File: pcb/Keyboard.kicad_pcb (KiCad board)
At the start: 2 copper layers, 166.7 x 94.8 mm, 63 parts

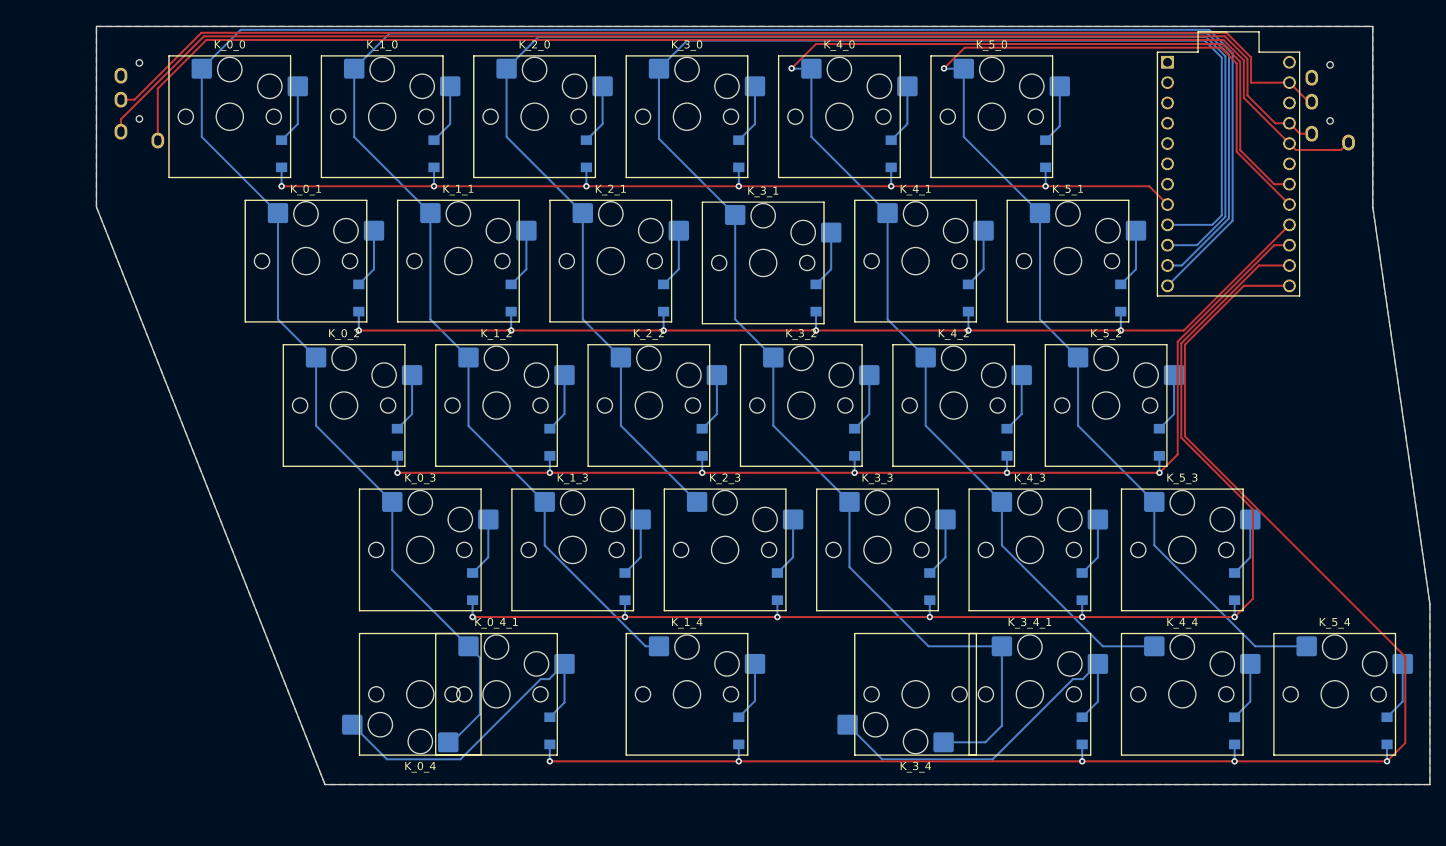
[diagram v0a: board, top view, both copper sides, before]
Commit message: Fix TRRS jack wiring.
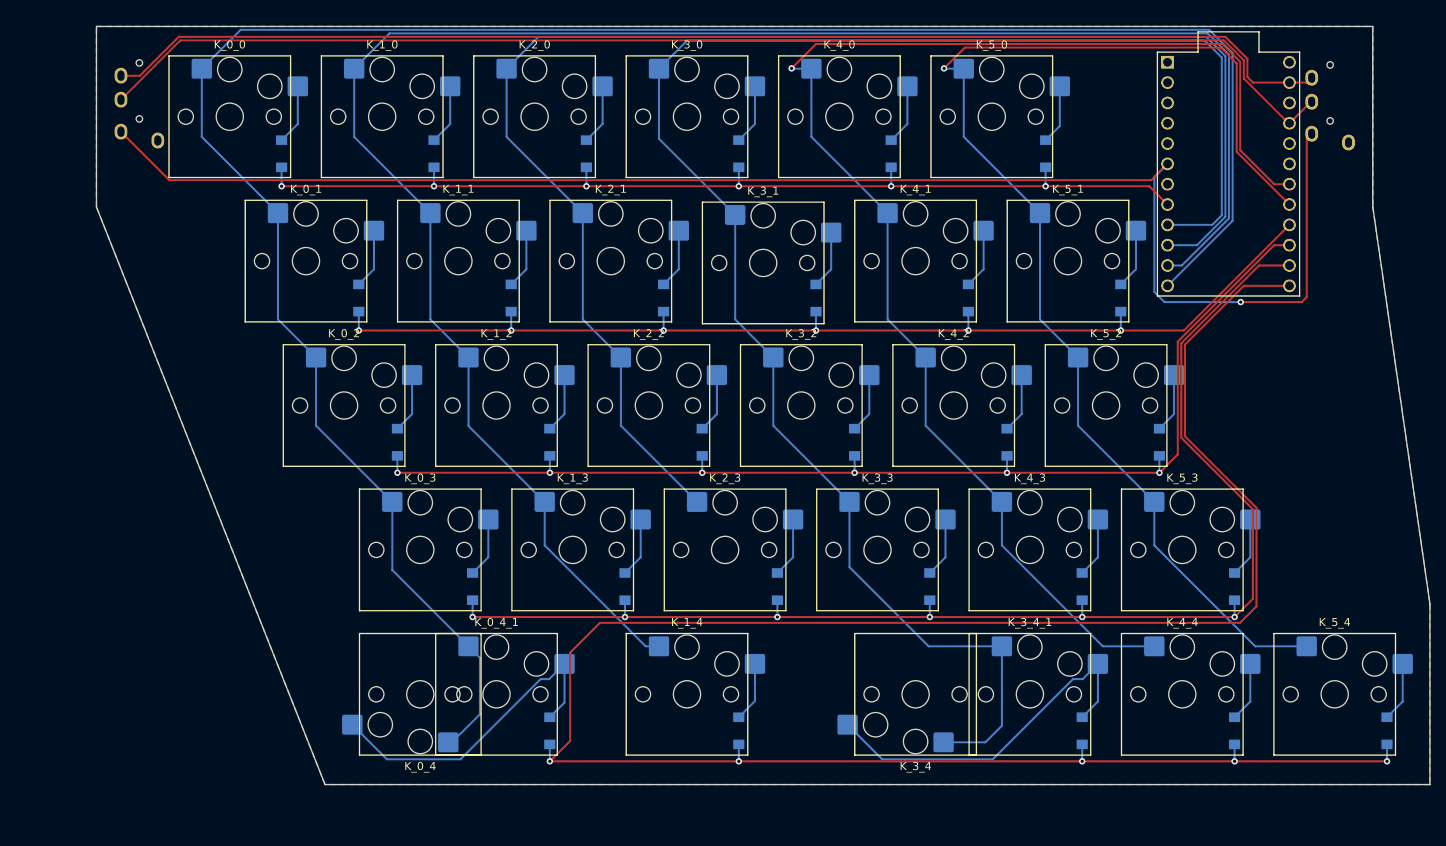
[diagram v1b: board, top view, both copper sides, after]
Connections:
- U_PROMICRO1 pad 20: Net-(U_PROMICRO1-Pad20) -> unconnected-(U_PROMICRO1-Pad20)
- U_PROMICRO1 pad 21: Net-(U_PROMICRO1-Pad21) -> trrs1
- U_PROMICRO1 pad 23: Net-(U_PROMICRO1-Pad23) -> trrs2
- U_PROMICRO1 pad 6: unconnected-(U_PROMICRO1-Pad6) -> trrs0
- U_TRRS1 pad 1: Net-(U_PROMICRO1-Pad20) -> unconnected-(U_TRRS1-Pad1)
- U_TRRS1 pad 2: Net-(U_PROMICRO1-Pad21) -> trrs0
- U_TRRS1 pad 3: Net-(U_PROMICRO1-Pad23) -> trrs1
- U_TRRS1 pad 4: unconnected-(U_TRRS1-Pad4) -> trrs2
- U_TRRS2 pad 1: Net-(U_PROMICRO1-Pad20) -> unconnected-(U_TRRS2-Pad1)
- U_TRRS2 pad 2: Net-(U_PROMICRO1-Pad21) -> trrs0
- U_TRRS2 pad 3: Net-(U_PROMICRO1-Pad23) -> trrs1
- U_TRRS2 pad 4: unconnected-(U_TRRS2-Pad4) -> trrs2
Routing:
- net trrs0: track 0.00 -> 191.4 mm, vias 0 -> 1
- net Net-(U_PROMICRO1-Pad20): track 166.7 -> 0.00 mm
- net Net-(U_PROMICRO1-Pad21): track 162.4 -> 0.00 mm
- net trrs1: track 0.00 -> 158.7 mm
- net Net-(U_PROMICRO1-Pad23): track 157.7 -> 0.00 mm
- net trrs2: track 0.00 -> 154.8 mm
- net row4: track 195.8 -> 270.6 mm

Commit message: wip
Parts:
- moved U_TRRS1 38.1 mm to (212.9, 71.9), turned to 90 degrees
- moved U_TRRS2 37.3 mm to (58.4, 71.8), turned to -90 degrees
- moved U_PROMICRO1 0.51 mm to (191.5, 50.5)
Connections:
- net trrs0 renamed trrs
- U_PROMICRO1 pad 21: trrs1 -> VCC
- U_PROMICRO1 pad 23: trrs2 -> GND
- U_TRRS1 pad 3: trrs1 -> GND
- U_TRRS1 pad 4: trrs2 -> VCC
- U_TRRS2 pad 3: trrs1 -> GND
- U_TRRS2 pad 4: trrs2 -> VCC
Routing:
- net VCC: track 0.00 -> 210.6 mm
- net GND: track 0.00 -> 195.4 mm, vias 0 -> 1
- net trrs1: track 158.7 -> 0.00 mm
- net trrs2: track 154.8 -> 0.00 mm
- net trrs: track 191.4 -> 179.2 mm, vias 1 -> 0
- net row0: track 125.9 -> 131.8 mm
- net row4: track 270.6 -> 273.1 mm
- net row3: track 164.3 -> 166.9 mm
- net row2: track 144.2 -> 146.7 mm
- net col0: track 265.0 -> 263.2 mm
- net row1: track 136.0 -> 137.8 mm
- net col1: track 231.8 -> 230.1 mm
- net col3: track 213.1 -> 211.3 mm
- net col2: track 185.3 -> 183.5 mm
- net col5: track 155.1 -> 155.6 mm
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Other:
- board size 166.7 x 94.8 mm -> 158.5 x 92.5 mm

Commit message: wip
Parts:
- moved D_3_4 32.3 mm to (141.1, 122.4)
- moved D_0_4 23.4 mm to (83.7, 124.1), turned to 180 degrees
- moved D_3_2 18.4 mm to (126.6, 86.2)
- moved D_2_2 18.3 mm to (107.6, 86.2)
- moved D_4_2 18.3 mm to (145.7, 86.2)
- moved D_1_2 18.3 mm to (88.5, 86.2)
- moved D_5_2 18.3 mm to (164.8, 86.2)
- moved D_5_0 18.2 mm to (150.5, 49.2)
- moved D_3_3 18.2 mm to (136.2, 104.2)
- moved D_4_1 18.2 mm to (140.9, 67.3)
- moved D_5_1 18.2 mm to (160.0, 67.3)
- moved D_5_4 18.2 mm to (193.4, 122.4)
- moved D_1_1 18.2 mm to (83.8, 67.3)
- moved D_5_3 18.2 mm to (174.3, 104.2)
- moved D_2_3 18.1 mm to (117.2, 104.2)
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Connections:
- U_PROMICRO1 pad 10: col2 -> col3
- U_PROMICRO1 pad 11: col1 -> col4
- U_PROMICRO1 pad 12: col0 -> col5
- U_PROMICRO1 pad 17: col5 -> row0
- U_PROMICRO1 pad 18: col4 -> unconnected-(U_PROMICRO1-Pad18)
- U_PROMICRO1 pad 7: unconnected-(U_PROMICRO1-Pad7) -> col0
- U_PROMICRO1 pad 8: row0 -> col1
- U_PROMICRO1 pad 9: col3 -> col2
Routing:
- net row4: track 273.1 -> 203.1 mm, vias 5 -> 0
- net col3: track 211.3 -> 163.9 mm, vias 0 -> 7
- net col0: track 263.2 -> 219.9 mm, vias 0 -> 7
- net col5: track 155.6 -> 123.6 mm, vias 1 -> 5
- net col1: track 230.1 -> 199.8 mm, vias 0 -> 6
- net row0: track 131.8 -> 160.5 mm, vias 6 -> 2
- net col2: track 183.5 -> 156.8 mm, vias 0 -> 5
- net col4: track 173.9 -> 147.4 mm, vias 1 -> 6
- net GND: track 195.4 -> 221.4 mm, vias 1 -> 2
- net row1: track 137.8 -> 147.0 mm, vias 6 -> 2
- net row3: track 166.9 -> 157.9 mm, vias 6 -> 0
- net trrs: track 179.2 -> 184.8 mm, vias 0 -> 1
- net Net-(D_3_4-Pad2): track 45.5 -> 40.5 mm
- net Net-(D_1_0-Pad2): track 7.57 -> 3.25 mm
- net Net-(D_2_0-Pad2): track 7.57 -> 3.29 mm
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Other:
- board size 158.5 x 92.5 mm -> 159.3 x 93.4 mm

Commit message: wip
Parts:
- moved D_4_4 2.11 mm to (174.4, 120.3)
- moved D_3_4 2.11 mm to (141.1, 120.3)
- moved D_5_4 2.09 mm to (193.5, 120.3)
- moved D_1_4 2.08 mm to (112.5, 120.3)
- moved U_PROMICRO1 2.00 mm to (204.4, 50.1)
- moved D_0_4 1.85 mm to (83.7, 122.2)
- moved U_TRRS1 1.54 mm to (213.8, 73.5)
- moved U_TRRS2 0.62 mm to (56.7, 73.5)
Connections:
- U_PROMICRO1 pad 10: col3 -> col1
- U_PROMICRO1 pad 11: col4 -> col2
- U_PROMICRO1 pad 12: col5 -> col3
- U_PROMICRO1 pad 16: row1 -> col5
- U_PROMICRO1 pad 17: row0 -> col4
- U_PROMICRO1 pad 2: unconnected-(U_PROMICRO1-Pad2) -> trrs
- U_PROMICRO1 pad 6: trrs -> unconnected-(U_PROMICRO1-Pad6)
- U_PROMICRO1 pad 7: col0 -> row0
- U_PROMICRO1 pad 8: col1 -> row1
- U_PROMICRO1 pad 9: col2 -> col0
- U_TRRS1 pad 2: trrs -> GND
- U_TRRS1 pad 3: GND -> trrs
- U_TRRS2 pad 2: trrs -> GND
- U_TRRS2 pad 3: GND -> trrs
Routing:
- net GND: track 221.4 -> 187.7 mm, vias 2 -> 1
- net VCC: track 206.6 -> 183.5 mm, vias 2 -> 1
- net col4: track 147.4 -> 170.4 mm
- net col5: track 123.6 -> 144.3 mm
- net row4: track 203.1 -> 191.6 mm
- net row1: track 147.0 -> 138.9 mm, vias 2 -> 0
- net row2: track 150.9 -> 153.2 mm
- net Net-(D_0_4-Pad2): track 37.9 -> 36.0 mm
- net col3: track 163.9 -> 162.0 mm
- net col0: track 219.9 -> 221.4 mm
- net row3: track 157.9 -> 159.1 mm
- net trrs: track 184.8 -> 185.6 mm
- net row0: track 160.5 -> 159.7 mm, vias 2 -> 0
- net Net-(D_5_4-Pad2): track 3.68 -> 2.89 mm
- net Net-(D_4_4-Pad2): track 3.64 -> 2.92 mm
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- removed copper zone on B.Cu, net GND
- removed copper zone on F.Cu, net GND
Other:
- board size 159.3 x 93.4 mm -> 157.4 x 89.6 mm

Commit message: wip
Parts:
- moved K_5_4 18.4 mm to (187.8, 122.0)
- moved K_5_1 18.4 mm to (154.5, 68.0)
- moved K_5_3 18.4 mm to (168.8, 104.0)
- moved K_5_0 18.4 mm to (145.0, 50.0)
- moved K_5_2 18.4 mm to (159.2, 86.0)
- moved K_4_4 18.3 mm to (168.8, 122.0)
- moved K_4_1 18.3 mm to (135.5, 68.0)
- moved K_4_0 18.3 mm to (126.0, 50.0)
- moved K_4_3 18.3 mm to (149.8, 104.0)
- moved K_4_2 18.3 mm to (140.2, 86.0)
- moved K_3_4_1 18.3 mm to (149.8, 122.0)
- moved K_3_1 18.3 mm to (116.5, 68.0)
- moved K_3_0 18.3 mm to (107.0, 50.0)
- moved K_3_3 18.3 mm to (130.8, 104.0)
- moved K_3_2 18.3 mm to (121.2, 86.0)
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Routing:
- net col1: track 200.2 -> 208.8 mm
- net col5: track 144.3 -> 150.0 mm
- net col2: track 156.0 -> 161.7 mm
- net col3: track 162.0 -> 167.5 mm
- net col0: track 221.4 -> 226.8 mm
- net row4: track 191.6 -> 196.2 mm
- net col4: track 170.4 -> 173.5 mm
- net trrs: track 185.6 -> 188.5 mm
- net row0: track 159.7 -> 162.0 mm
- net VCC: track 183.5 -> 184.3 mm
- net GND: track 187.7 -> 188.5 mm
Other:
- board size 157.4 x 89.6 mm -> 157.8 x 90 mm
